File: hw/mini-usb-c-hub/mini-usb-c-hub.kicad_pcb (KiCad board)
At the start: 4 copper layers, 56 x 30 mm, 35 parts, among them J101 USB_C_Receptacle_USB2.0_16P, J201 USB_A, J301 USB_A, P101 USB_C_Plug_USB3.0, U101 FE1.1s, Y101 12MHz

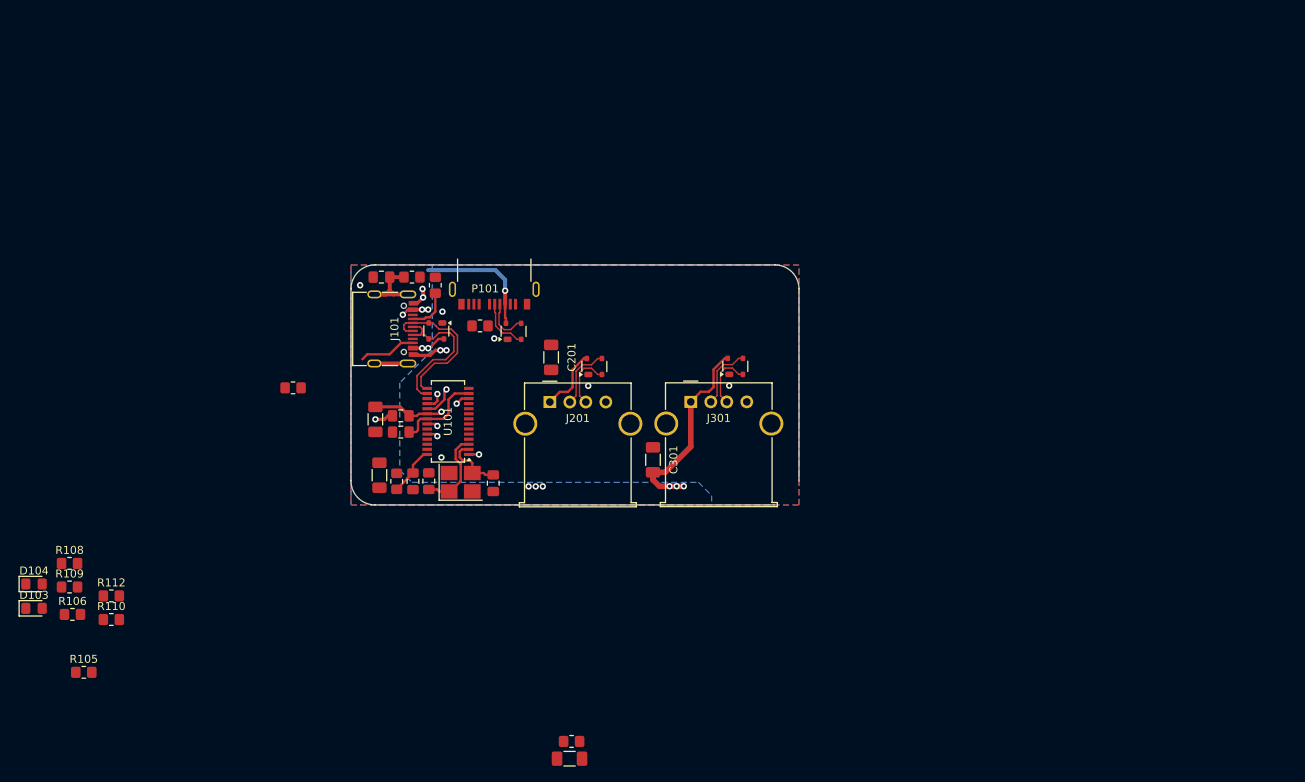
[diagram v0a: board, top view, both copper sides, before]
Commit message: chore(hw): layout around switch and add downstream USB-C
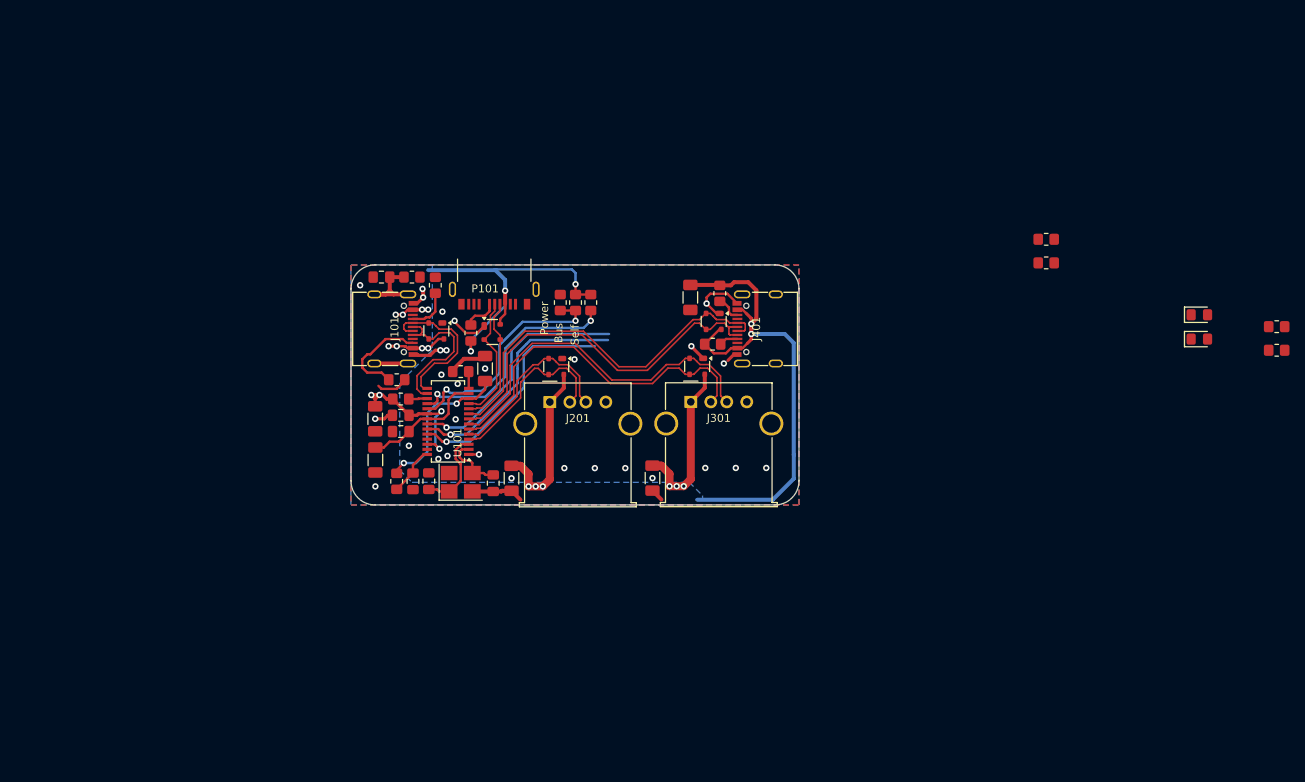
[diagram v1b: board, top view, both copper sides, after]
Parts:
- added C401: 10u, Capacitor_SMD:C_1206_3216Metric_Pad1.33x1.80mm_HandSolder, F.Cu at (156.7, 93.0)
- added D401: PRTR5V0U2X, Package_TO_SOT_SMD:SOT-143, F.Cu at (159.6, 96.0)
- added J401: USB_C_Receptacle_USB2.0_16P, local:USB_C_Receptacle_G-Switch_GT-USB-7010ASV_shortened, F.Cu at (166.3, 96.9)
- added R113: 300R, Resistor_SMD:R_0805_2012Metric_Pad1.20x1.40mm_HandSolder, F.Cu at (201.2, 85.7)
- added R114: 300R, Resistor_SMD:R_0805_2012Metric_Pad1.20x1.40mm_HandSolder, F.Cu at (201.2, 88.6)
- added R401: ?, Resistor_SMD:R_0805_2012Metric_Pad1.20x1.40mm_HandSolder, F.Cu at (159.5, 98.8)
- added R402: ?, Resistor_SMD:R_0805_2012Metric_Pad1.20x1.40mm_HandSolder, F.Cu at (160.4, 92.5)
- moved R110 149.5 mm to (230.0, 99.6)
- moved R112 149.5 mm to (230.0, 96.6)
- moved D103 149.5 mm to (220.3, 98.2)
- moved D104 149.5 mm to (220.3, 95.1)
- moved R105 78.4 mm to (144.3, 93.6), turned to -90 degrees
- moved R108 71.2 mm to (142.4, 93.6), turned to -90 degrees
- moved R109 70.9 mm to (140.5, 93.6), turned to -90 degrees
- moved C104 49.9 mm to (131.1, 101.9), turned to 90 degrees
- moved R106 49.1 mm to (120.5, 105.7)
- moved R111 48.3 mm to (128.0, 102.2)
- moved C201 15.9 mm to (134.4, 115.6), turned to -90 degrees
- moved R102 13.0 mm to (120.0, 103.3)
- moved D201 4.77 mm to (140.0, 101.6), turned to -90 degrees
- moved D301 4.77 mm to (157.6, 101.6), turned to -90 degrees
- moved D102 2.67 mm to (132.0, 97.3), turned to 0 degrees
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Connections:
- D201 pad 2: /D3USB+ -> /D4USB+
- D201 pad 3: /D3USB- -> /D4USB-
- D301 pad 2: /D2USB+ -> /D3USB+
- D301 pad 3: /D2USB- -> /D3USB-
- J201 pad 2: /D3USB- -> /D4USB-
- J201 pad 3: /D3USB+ -> /D4USB+
- J301 pad 2: /D2USB- -> /D3USB-
- J301 pad 3: /D2USB+ -> /D3USB+
- U101 pad 23: unconnected-(U101-LED1/EESCL-Pad23) -> Net-(U101-LED1/EESCL)
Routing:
- net +5V: track 65.4 -> 180.1 mm, vias 13 -> 23
- net /D2USB+: track 7.36 -> 48.6 mm
- net /D2USB-: track 8.07 -> 48.8 mm
- net /D3USB+: track 7.36 -> 45.3 mm
- net /D3USB-: track 8.07 -> 44.5 mm
- net GND: track 10.7 -> 43.6 mm, vias 12 -> 29
- net Net-(U101-LED1/EESCL): track 0.00 -> 30.0 mm, vias 0 -> 1
- net Net-(U101-DRV): track 1.38 -> 29.9 mm
- net Net-(D103-K): track 1.38 -> 28.7 mm
- net Net-(U101-VBUSM): track 2.28 -> 28.9 mm, vias 1 -> 2
- net Net-(U101-BUSJ): track 4.01 -> 29.3 mm, vias 1 -> 2
- net /D4USB+: track 0.00 -> 23.5 mm
- net /D4USB-: track 0.00 -> 22.7 mm
- net Net-(U101-VD18_O): track 1.78 -> 19.5 mm, vias 1 -> 2
- net /D1USB-: track 5.94 -> 16.2 mm
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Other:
- board text added: "Bus"
- board text added: "Power"
- board text added: "Self"

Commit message: chore(hw): improve layout
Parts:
- removed R113: 300R, Resistor_SMD:R_0805_2012Metric_Pad1.20x1.40mm_HandSolder
- moved C102 3.12 mm to (120.1, 111.9), turned to 180 degrees
- moved R104 1.35 mm to (119.1, 114.9)
- moved C105 1.02 mm to (121.9, 114.9)
- moved C106 0.25 mm to (131.8, 116.2)
- moved C107 0.18 mm to (124.2, 116.0)
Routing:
- net GND: track 43.6 -> 71.9 mm, vias 29 -> 28
- net +5V: track 180.1 -> 183.4 mm
- net +3.3V: track 15.6 -> 13.0 mm

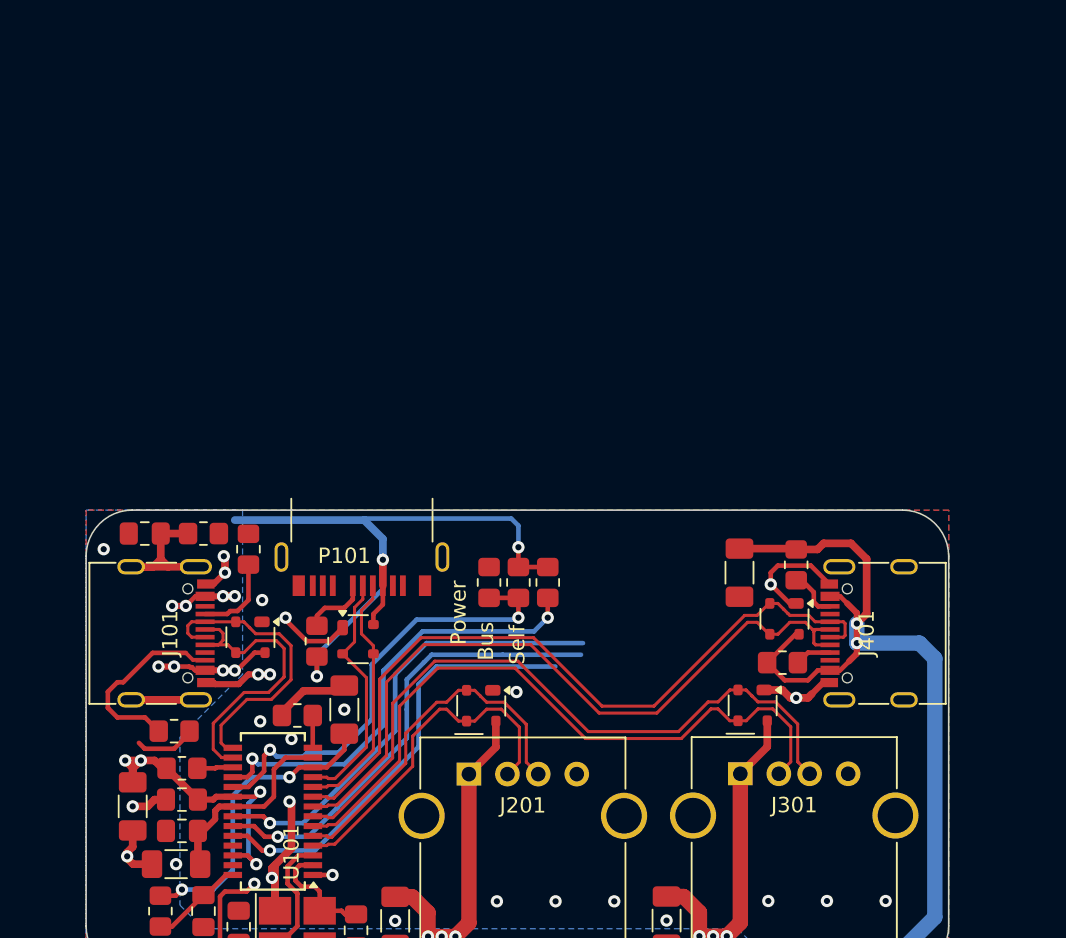
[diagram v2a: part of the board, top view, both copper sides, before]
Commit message: chore(hw): replace USB-C plug with socket
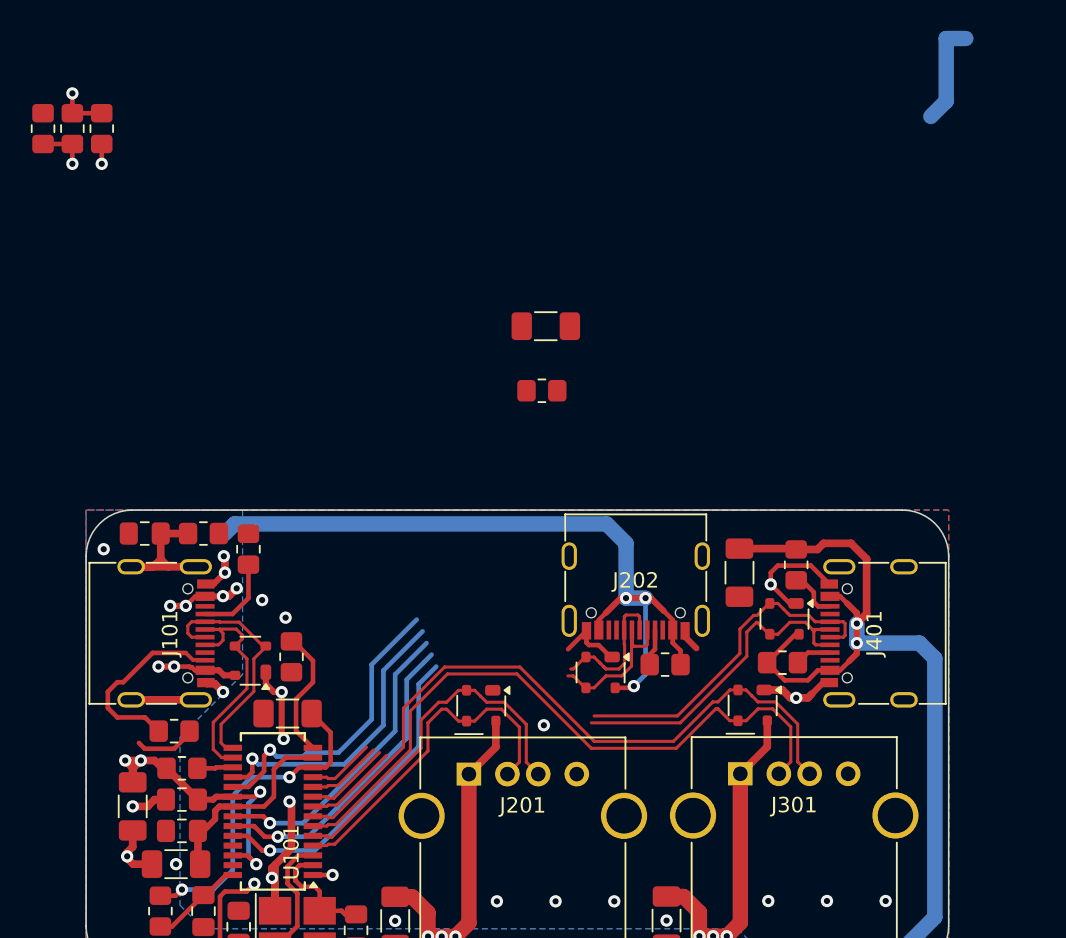
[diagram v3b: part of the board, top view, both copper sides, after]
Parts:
- removed D102: PRTR5V0U2X, Package_TO_SOT_SMD:SOT-143
- removed P101: USB_C_Plug_USB3.0, local:USB_C_Plug_G-Switch_GT-USB-8016A
- removed R107: ?, Resistor_SMD:R_0805_2012Metric_Pad1.20x1.40mm_HandSolder
- added C202: 10u, Capacitor_SMD:C_1206_3216Metric_Pad1.33x1.80mm_HandSolder, F.Cu at (144.1, 77.0)
- added D202: PRTR5V0U2X, Package_TO_SOT_SMD:SOT-143, F.Cu at (147.7, 99.4)
- added J202: USB_C_Receptacle_USB2.0_16P, local:USB_C_Receptacle_G-Switch_GT-USB-7010ASV_shortened, F.Cu at (150.0, 93.0)
- added R201: ?, Resistor_SMD:R_0805_2012Metric_Pad1.20x1.40mm_HandSolder, F.Cu at (143.9, 81.2)
- added R202: ?, Resistor_SMD:R_0805_2012Metric_Pad1.20x1.40mm_HandSolder, F.Cu at (151.9, 98.9)
- moved R105 41.3 mm to (115.3, 64.1)
- moved R108 41.3 mm to (113.4, 64.1)
- moved R109 41.3 mm to (111.5, 64.1)
- moved R111 3.83 mm to (127.6, 98.4), turned to 90 degrees
- moved C104 3.69 mm to (127.4, 102.1), turned to 180 degrees
- moved D101 1.52 mm to (125.0, 98.7), turned to 180 degrees
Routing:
- net /D2USB+: track 48.6 -> 28.2 mm
- net /D2USB-: track 48.8 -> 29.1 mm
- net +5V: track 183.4 -> 198.7 mm, vias 23 -> 22
- net Net-(U101-DRV): track 29.9 -> 19.8 mm
- net Net-(U101-LED1/EESCL): track 30.0 -> 20.3 mm
- net Net-(U101-VBUSM): track 28.9 -> 20.4 mm
- net Net-(D103-K): track 28.7 -> 20.9 mm
- net Net-(U101-BUSJ): track 29.3 -> 22.7 mm
- net Net-(U101-REXT): track 2.10 -> 8.48 mm
- net Net-(P101-CC): track 4.31 -> 0.00 mm
- net /UUSB+: track 19.8 -> 15.9 mm
- net /UUSB-: track 19.2 -> 15.9 mm
- net Net-(J202-CC1): track 0.00 -> 2.39 mm
- net /D1USB+: track 16.0 -> 13.7 mm
- net GND: track 71.9 -> 70.1 mm, vias 28 -> 26
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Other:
- board text removed: "Bus"
- board text removed: "Power"
- board text removed: "Self"

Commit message: chore(hw): update layout, fix references
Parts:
- added D101: LED, LED_SMD:LED_0805_2012Metric_Pad1.15x1.40mm_HandSolder, F.Cu at (134.2, 91.6)
- added D102: LED, LED_SMD:LED_0805_2012Metric_Pad1.15x1.40mm_HandSolder, F.Cu at (138.3, 91.6)
- added D104: LED, LED_SMD:LED_0805_2012Metric_Pad1.15x1.40mm_HandSolder, F.Cu at (134.2, 93.9)
- moved R102 99.1 mm to (131.2, 92.5), turned to 90 degrees
- moved D103 82.2 mm to (138.3, 93.9)
- moved R101 69.0 mm to (132.6, 96.0)
- moved R103 66.5 mm to (166.3, 77.6)
- moved D105 60.5 mm to (161.3, 82.2), turned to 180 degrees
- moved R108 32.9 mm to (126.6, 94.2)
- moved R110 32.9 mm to (128.5, 94.2)
- moved R109 30.7 mm to (125.7, 91.3), turned to 0 degrees
- moved C201 16.5 mm to (143.4, 93.5), turned to 90 degrees
- moved R201 12.0 mm to (141.2, 92.8), turned to -90 degrees
- moved R105 2.80 mm to (124.7, 94.2)
- moved C104 0.61 mm to (131.8, 115.6)
- moved D201 0.54 mm to (147.3, 99.8)
- moved C105 0.38 mm to (124.2, 115.6)
- renumbered C108 to C102, C109 to C103, C106 to C104, C107 to C105, C102 to C106, C103 to C107, C104 to C108, C105 to C109, C202 to C201, C401 to C301, C301 to C401, C201 to C501, D104 to D105, D101 to D106, D202 to D201, D401 to D301, D301 to D401, D201 to D501, J202 to J201, J401 to J301, J301 to J401, J201 to J501, R114 to R101, R110 to R102, R112 to R103, R103 to R104, R101 to R105, R102 to R106, R106 to R107, R105 to R110, R104 to R112, R402 to R301, R401 to R302
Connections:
- net Net-(U101-LED1/EESCL) renamed /LED1
- D103 pad 1: Net-(D103-K) -> /DRV
- D103 pad 2: Net-(D103-A) -> Net-(D101-K)
- R101 pad 2: unconnected-(R114-Pad2) -> Net-(D101-K)
- R102 pad 1: Net-(D103-A) -> /LED2
- R102 pad 2: Net-(U101-DRV) -> Net-(D102-K)
- R103 pad 1: Net-(U101-DRV) -> /DRV
- U101 pad 22: Net-(U101-DRV) -> /DRV
- U101 pad 24: Net-(D103-K) -> /LED2
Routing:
- net /DRV: track 0.00 -> 31.2 mm, vias 0 -> 2
- net GND: track 70.1 -> 95.0 mm, vias 26 -> 21
- net Net-(D103-K): track 20.9 -> 0.00 mm, vias 1 -> 0
- net /D2USB+: track 28.2 -> 48.7 mm
- net /D1USB+: track 13.7 -> 33.9 mm
- net /D1USB-: track 15.2 -> 35.4 mm
- net /D2USB-: track 29.1 -> 48.9 mm
- net Net-(U101-DRV): track 19.8 -> 0.00 mm, vias 1 -> 0
- net /LED1: track 20.3 -> 5.19 mm
- net Net-(J201-CC2): track 0.00 -> 13.6 mm, vias 0 -> 2
- net Net-(D102-K): track 0.00 -> 11.1 mm
- net +5V: track 198.7 -> 208.3 mm
- net Net-(D101-K): track 0.00 -> 9.26 mm
- net /LED2: track 0.00 -> 5.73 mm, vias 0 -> 1
- net Net-(U101-VBUSM): track 20.4 -> 16.5 mm
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
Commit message: chore(hw): first complete layout
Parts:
- moved R103 38.3 mm to (130.8, 92.2), turned to 90 degrees
- moved D105 30.1 mm to (133.0, 92.2), turned to -90 degrees
- moved R201 12.5 mm to (150.9, 100.8), turned to 180 degrees
- moved R102 2.85 mm to (132.2, 95.1), turned to 0 degrees
- moved D101 2.03 mm to (136.3, 91.6)
- moved D102 2.03 mm to (140.3, 91.6)
- moved D103 2.03 mm to (140.3, 93.9)
- moved D104 2.03 mm to (136.3, 93.9)
- moved R101 1.09 mm to (132.2, 97.0)
- moved R202 0.63 mm to (152.5, 98.9)
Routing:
- net /LED1: track 5.19 -> 47.3 mm, vias 1 -> 2
- net /LED2: track 5.73 -> 47.6 mm, vias 1 -> 2
- net /DRV: track 31.2 -> 40.9 mm, vias 2 -> 3
- net Net-(D101-K): track 9.26 -> 15.8 mm
- net Net-(J201-CC2): track 13.6 -> 10.3 mm
- net Net-(D105-A): track 0.00 -> 3.00 mm
- net Net-(J101-SHIELD): track 23.3 -> 26.1 mm
- net Net-(D102-K): track 11.1 -> 13.7 mm
- net +5V: track 208.3 -> 209.6 mm
- net /UUSB-: track 15.9 -> 17.0 mm
- net Net-(J101-CC2): track 12.5 -> 13.5 mm
- net GND: track 95.0 -> 94.1 mm, vias 21 -> 35
- net /D4USB-: track 22.6 -> 23.3 mm
- net /D3USB-: track 44.1 -> 44.9 mm
- net /D1USB+: track 33.9 -> 34.5 mm
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
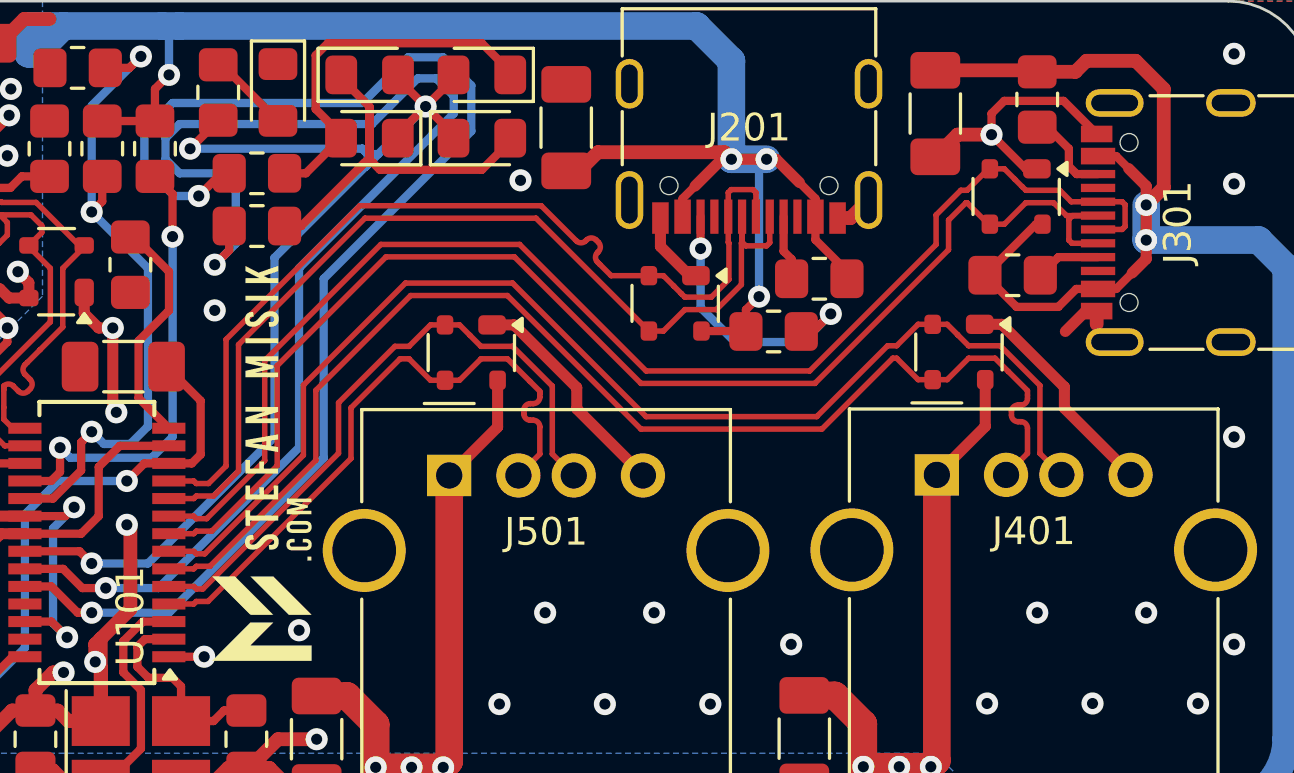
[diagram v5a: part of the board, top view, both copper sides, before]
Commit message: refactor(hw): use 0.17 mm width for USB pairs
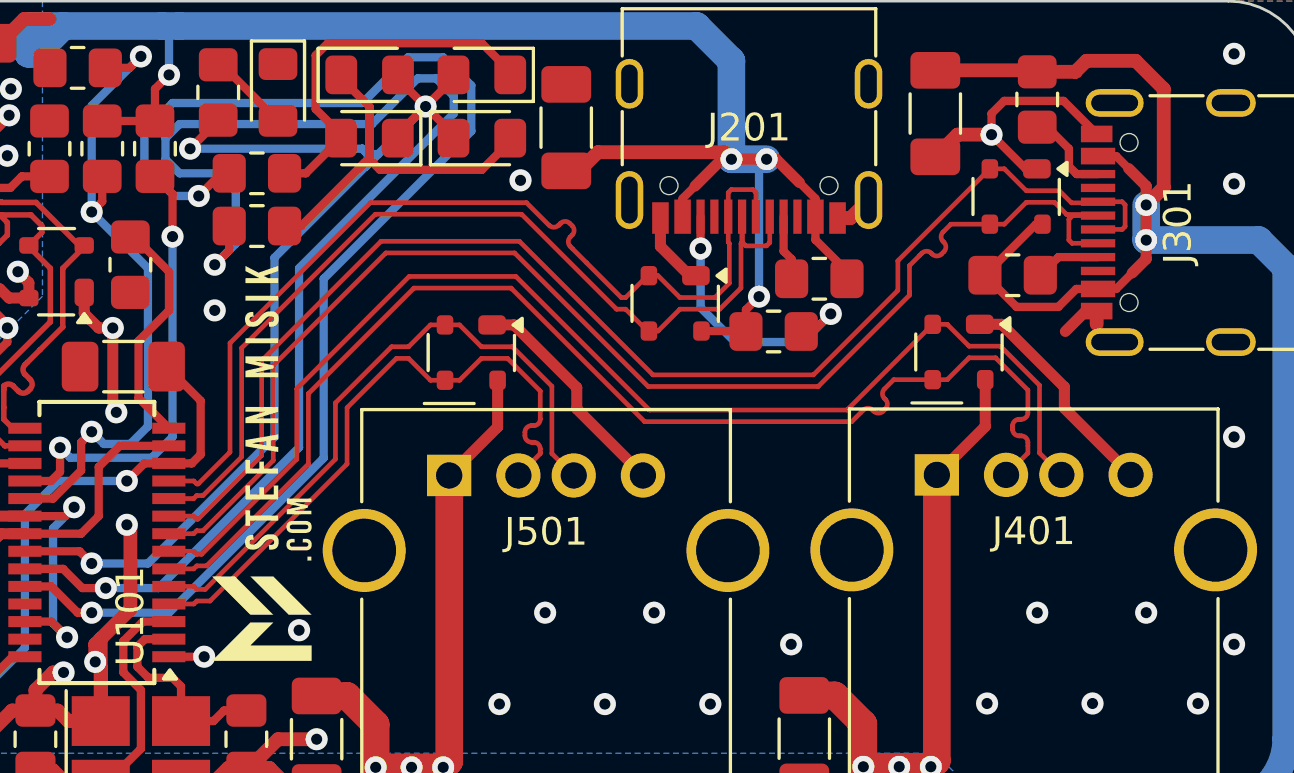
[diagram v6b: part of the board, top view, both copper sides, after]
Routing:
- net /D1USB+: track 34.5 -> 35.1 mm

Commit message: refactor(hw): minor fixes
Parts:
- moved C201 0.38 mm to (143.4, 93.1)
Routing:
- net GND: track 94.1 -> 96.6 mm, vias 35 -> 41
- net /D1USB+: track 35.1 -> 34.3 mm
